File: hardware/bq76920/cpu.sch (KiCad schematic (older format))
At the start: 1 part

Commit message: initial commit
Signed-off-by: Ene Alexandru <ene.alexandru@gmail.com>
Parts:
- removed U?: STM32F030K6Tx, Package_QFP:LQFP-32_7x7mm_P0.8mm, symbol MCU_ST_STM32F0:STM32F030K6Tx
- added U?: STM32L031F4Px, Package_SO:TSSOP-20_4.4x6.5mm_P0.65mm, symbol MCU_ST_STM32L0:STM32L031F4Px
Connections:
- net labels removed: GND
- wire segments 4 -> 0
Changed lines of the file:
@@
 EESchema Schematic File Version 4
 LIBS:bq76920-cache
-EELAYER 29 0
+EELAYER 26 0
 EELAYER END
 $Descr A4 11693 8268
 encoding utf-8
-Sheet 6 6
+Sheet 4 4
 Title ""
 Date ""
@@
 Comment4 ""
 $EndDescr
-$Comp
-L MCU_ST_STM32F0:STM32F030K6Tx U?
-U 1 1 5D5C73B0
-P 5150 3450
-F 0 "U?" H 4700 2500 50  0000 C CNN
-F 1 "STM32F030K6Tx" H 5550 2500 50  0000 C CNN
-F 2 "Package_QFP:LQFP-32_7x7mm_P0.8mm" H 4650 2550 50  0001 R CNN
-F 3 "http://www.st.com/st-web-ui/static/active/en/resource/technical/document/datasheet/DM00088500.pdf" H 5150 3450 50  0001 C CNN
-	1    5150 3450
-	1    0    0    -1
-$EndComp
 Text HLabel 1150 900  0    50   Input ~ 0
 VCC_3V3
@@
 PACK_SDA
 $Comp
-L power:GND #PWR?
-U 1 1 5D5C9390
-P 5050 4550
-F 0 "#PWR?" H 5050 4300 50  0001 C CNN
-F 1 "GND" H 5055 4377 50  0000 C CNN
-F 2 "" H 5050 4550 50  0001 C CNN
-F 3 "" H 5050 4550 50  0001 C CNN
-	1    5050 4550
+L MCU_ST_STM32L0:STM32L031F4Px U?
+U 1 1 5E142A54
+P 3950 2900
+F 0 "U?" H 3950 2014 50  0000 C CNN
+F 1 "STM32L031F4Px" H 3950 1923 50  0000 C CNN
+F 2 "Package_SO:TSSOP-20_4.4x6.5mm_P0.65mm" H 3550 2200 50  0001 R CNN
+F 3 "http://www.st.com/st-web-ui/static/active/en/resource/technical/document/datasheet/DM00140359.pdf" H 3950 2900 50  0001 C CNN
+	1    3950 2900
 	1    0    0    -1
 $EndComp
-Wire Wire Line
-	5050 4450 5050 4500
-Wire Wire Line
-	5050 4500 5150 4500
-Wire Wire Line
-	5150 4500 5150 4450
-Connection ~ 5050 4500
-Wire Wire Line
-	5050 4500 5050 4550
 $EndSCHEMATC

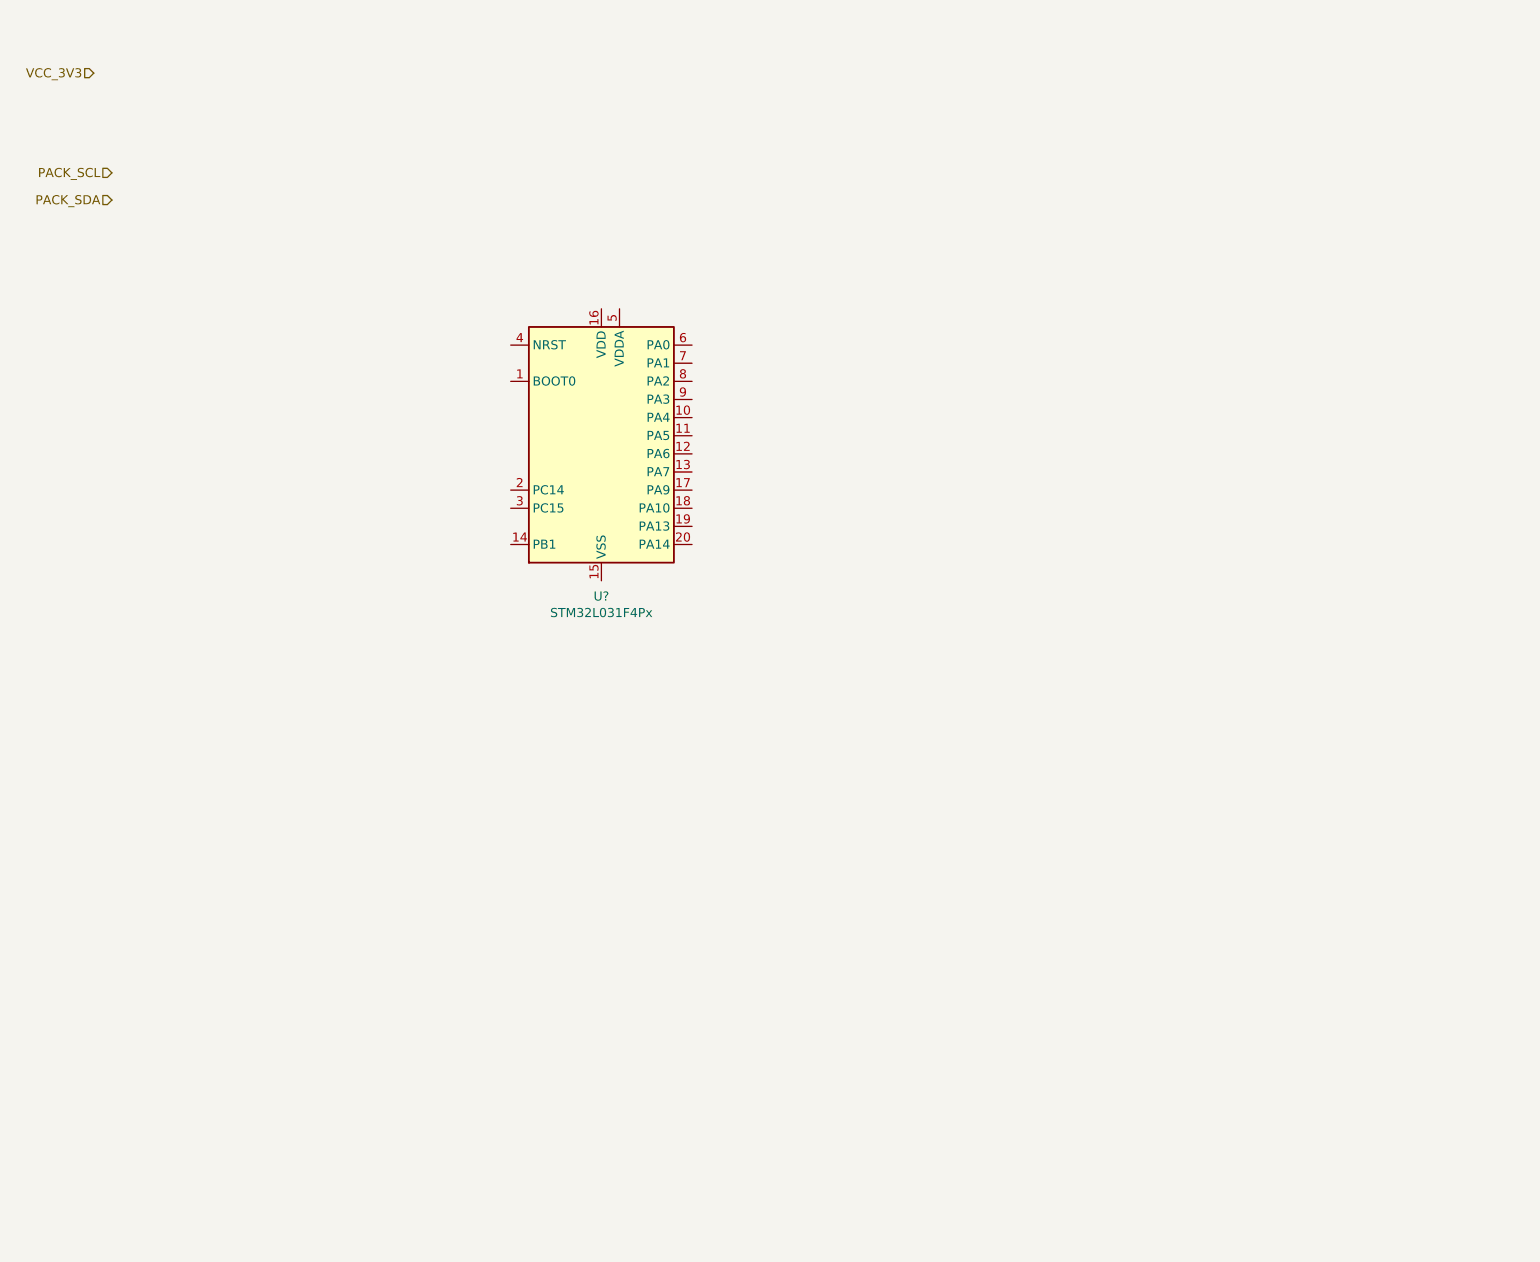
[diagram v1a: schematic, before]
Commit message: update cpu and reduce BOM
Signed-off-by: Ene Alexandru <ene.alexandru@gmail.com>
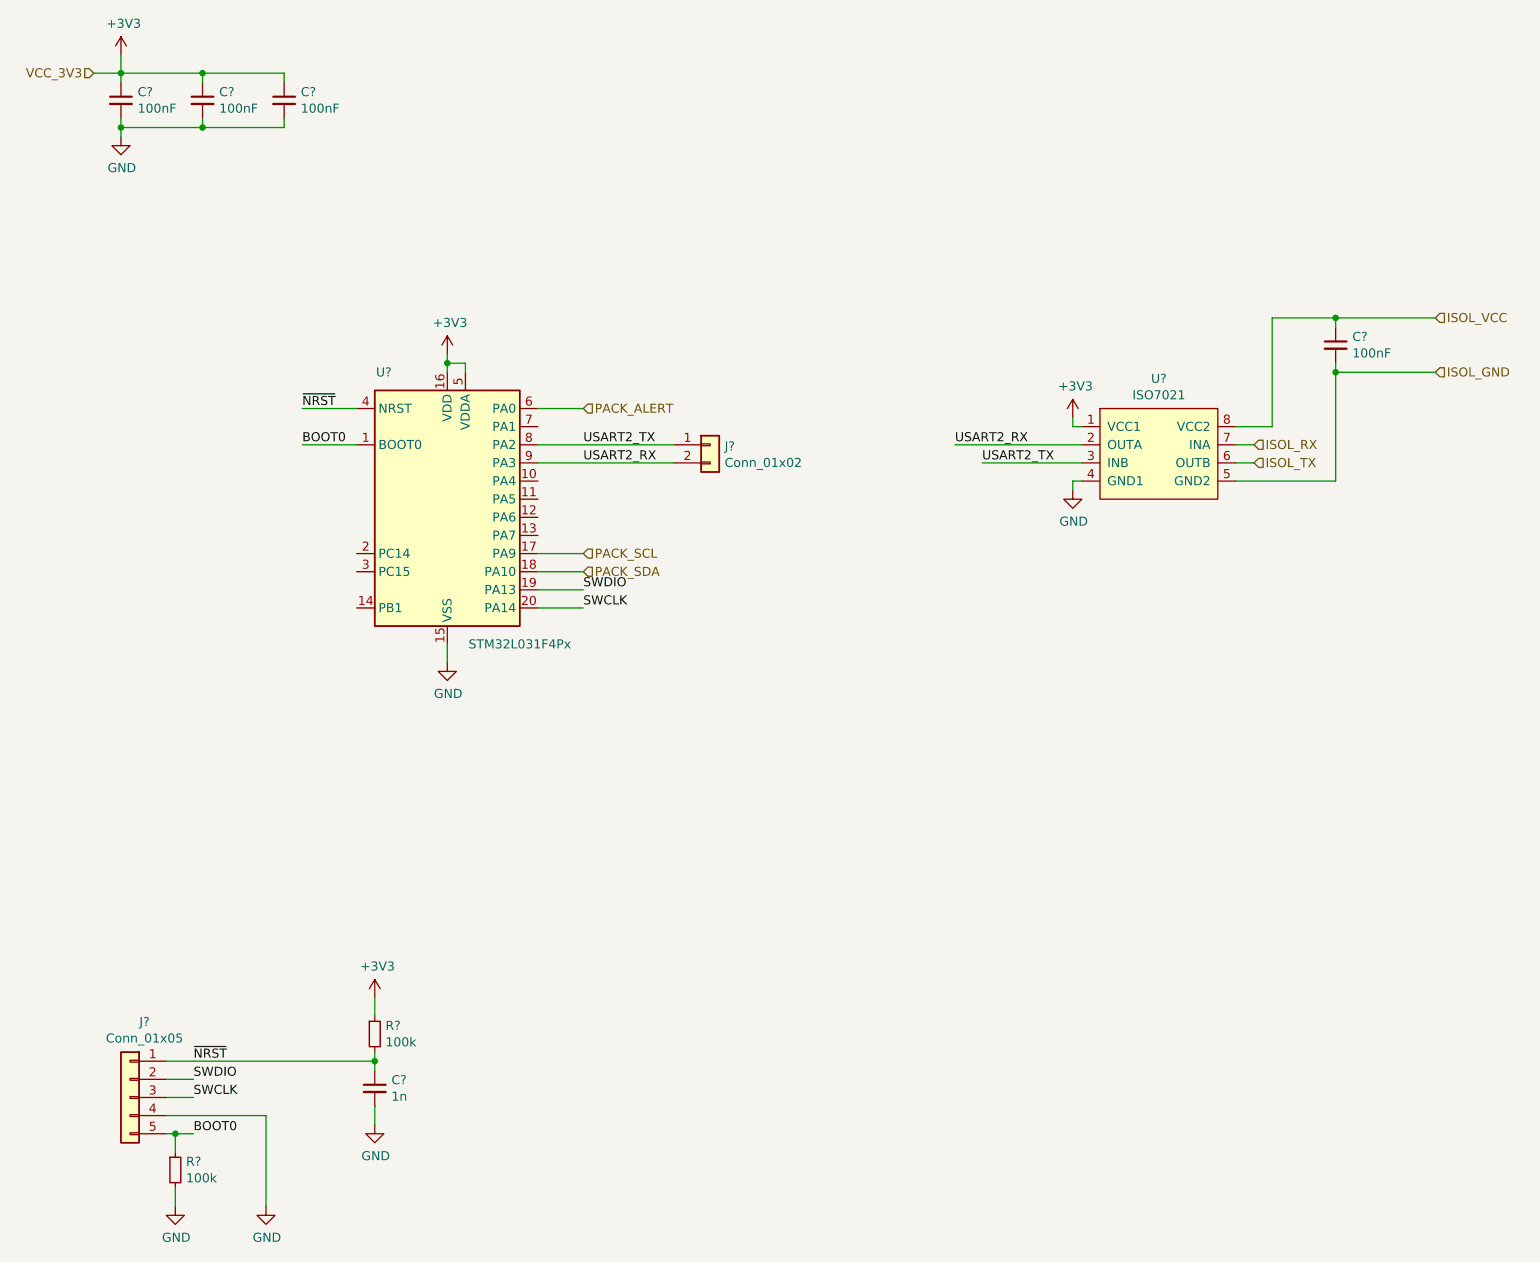
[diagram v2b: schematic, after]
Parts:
- added C?: 1n, symbol Device:C_Small
- added C? (x4): 100nF, symbol Device:C_Small
- added J?: Conn_01x05, symbol Connector_Generic:Conn_01x05
- added J?: Conn_01x02, symbol Connector_Generic:Conn_01x02
- added R? (x2): 100k, symbol Device:R_Small
- added U?: ISO7021, symbol bq769xx:ISO7021
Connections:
- net PACK_SCL: now also U?.17 (PA9)
- net PACK_SDA: now also U?.18 (PA10)
- net BOOT0: now reaches U?.1 (BOOT0)
- net BOOT0: now also J?.5 (Pin_5), R?.1
- net GND: now reaches U?.15 (VSS)
- net GND: now also C?.2, C?.2, C?.2, C?.2, J?.4 (Pin_4), R?.2, U?.4 (GND1)
- net +3V3: now reaches U?.16 (VDD)
- net +3V3: now also U?.5 (VDDA), C?.1, C?.1, C?.1, R?.1, U?.1 (VCC1)
- net SWDIO: now reaches U?.19 (PA13)
- net SWDIO: now also J?.2 (Pin_2)
- net SWCLK: now reaches U?.20 (PA14)
- net SWCLK: now also J?.3 (Pin_3)
- net ~NRST: now reaches U?.4 (NRST)
- net ~NRST: now also C?.1, J?.1 (Pin_1), R?.2
- net PACK_ALERT: now reaches U?.6 (PA0)
- net USART2_TX: now reaches U?.8 (PA2)
- net USART2_TX: now also J?.1 (Pin_1), U?.3 (INB)
- net USART2_RX: now reaches U?.9 (PA3)
- net USART2_RX: now also J?.2 (Pin_2), U?.2 (OUTA)
- new net ISOL_GND: C?.2, U?.5 (GND2)
- new net ISOL_RX: U?.7 (INA)
- new net ISOL_TX: U?.6 (OUTB)
- new net ISOL_VCC: C?.1, U?.8 (VCC2)
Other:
- moved on the sheet: U?

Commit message: update bom
Signed-off-by: Ene Alexandru <ene.alexandru@gmail.com>
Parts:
- R? (x2): value 100k -> 10k
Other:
- moved on the sheet: C?, J?, U?
